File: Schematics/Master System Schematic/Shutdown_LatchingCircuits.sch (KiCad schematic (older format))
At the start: 6 parts, among them K1 3PoleSwitchingRelay, K2 3PoleSwitchingRelay, SW5 IMD_LatchReset, SW6 BMS_LatchReset

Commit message: General cleanup, and fixes
>Shutdown latch circuits updated
>Shutdown latch resets updated
>BMS cleaned up
>Some wire runs cleaned up
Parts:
- removed SW5: IMD_LatchReset, symbol Switch:SW_Push
- removed SW6: BMS_LatchReset, symbol Switch:SW_Push
- added R? (x2): 500, symbol Device:R
- D1, D2: symbol Diode:1N4001 -> LatchingFaultBoard-rescue:1N4001-Diode-Shutdown-rescue
- K1, K2: symbol NER:3PoleSwitchingRelay -> LatchingFaultBoard-rescue:3PoleSwitchingRelay-FSAE_Components-Shutdown-rescue
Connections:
- net IMDErrorIndicatorControl_OUT is gone; now on net GLV+_Fused: K1.9
- net IMD_Latch_Reset-: now reaches D1.1 (K), K1.1, K1.5
- net BMS_Latch_Reset-: now reaches D2.1 (K), K2.1, K2.5
- net BMSErrorIndicatorControl_IN: no longer names the net of K2.10
- net BMSErrorIndicatorControl_IN: now also R?.1
- net BMSErrorIndicatorControl_OUT renamed GLV+_Fused
- net BMS_Status renamed BMS_Latch_Reset+
- net IMDErrorIndicatorControl_IN: no longer names the net of K1.10
- net IMDErrorIndicatorControl_IN: now also R?.1
- net IMD_Status renamed IMD_Latch_Reset+
- net ShutdownLatch_Control_IN renamed Shutdown_OUT
- net ShutdownLatch_Control_OUT renamed Shutdown_IN
- new net BMS_Fault_Indicator: R?.2
- new net IMD_Fault_Indicator: R?.2
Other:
- note added: "Latching Fault Circuit PCB"
- note removed: "Active-High Output Relay Latch"
- moved on the sheet: D1, D2, K1, K2

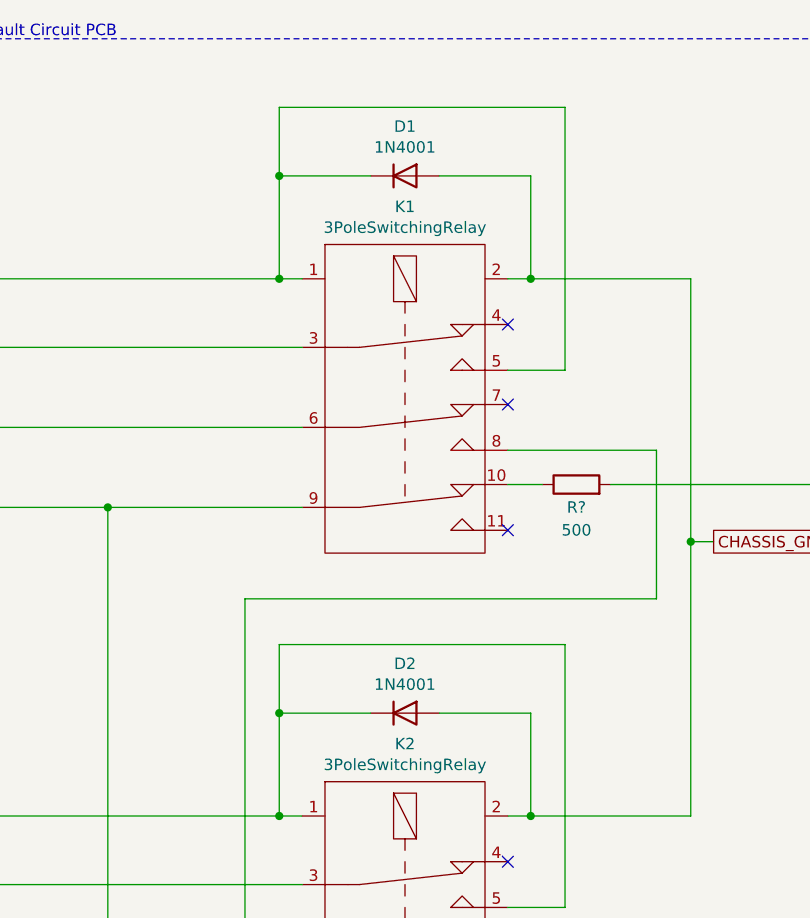
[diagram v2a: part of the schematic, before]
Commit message: Fixed symbol library issues
>Migrated 3polerelay to NER and replaced in schematic
>Used built in Diode instead of custom diode
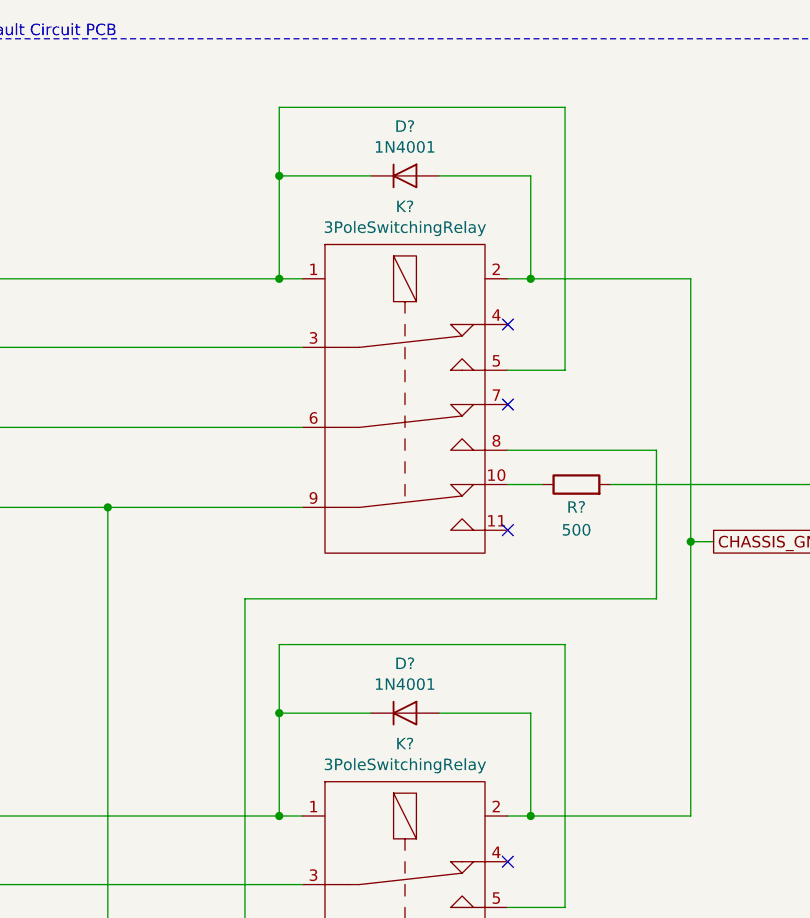
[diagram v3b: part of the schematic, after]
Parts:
- removed D1, D2: 1N4001, Diode_THT:D_DO-41_SOD81_P10.16mm_Horizontal, symbol LatchingFaultBoard-rescue:1N4001-Diode-Shutdown-rescue
- removed K1, K2: 3PoleSwitchingRelay, symbol LatchingFaultBoard-rescue:3PoleSwitchingRelay-FSAE_Components-Shutdown-rescue
- added D? (x2): 1N4001, Diode_THT:D_DO-41_SOD81_P10.16mm_Horizontal, symbol Diode:1N4001
- added K? (x2): 3PoleSwitchingRelay, symbol NER:3PoleSwitchingRelay
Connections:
- net BMS_Latch_Reset+: now also K?.3
- net BMS_Latch_Reset-: now also D?.1 (K), K?.1, K?.5
- net CHASSIS_GND: now also D?.2 (A), D?.2 (A), K?.2, K?.2
- net GLV+_Fused: now also K?.9, K?.9
- net IMD_Latch_Reset+: now also K?.3
- net IMD_Latch_Reset-: now also D?.1 (K), K?.1, K?.5
- net Shutdown_IN: now also K?.6
- net Shutdown_OUT: now also K?.8
- net at R?.1: now also K?.10 (x2)
- new net: K?.6, K?.8
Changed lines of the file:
@@
 Wire Wire Line
 	4800 2850 5050 2850
-$Comp
-L LatchingFaultBoard-rescue:1N4001-Diode-Shutdown-rescue D1
-U 1 1 5DDE3BD5
-P 4350 2000
-F 0 "D1" H 4350 2216 50  0000 C CNN
-F 1 "1N4001" H 4350 2125 50  0000 C CNN
-F 2 "Diode_THT:D_DO-41_SOD81_P10.16mm_Horizontal" H 4350 1825 50  0001 C CNN
-F 3 "http://www.vishay.com/docs/88503/1n4001.pdf" H 4350 2000 50  0001 C CNN
-	1    4350 2000
-	1    0    0    -1
-$EndComp
 Wire Wire Line
 	3800 2000 4200 2000
@@
 Wire Wire Line
 	3800 1700 5050 1700
-$Comp
-L LatchingFaultBoard-rescue:3PoleSwitchingRelay-FSAE_Components-Shutdown-rescue K2
-U 1 1 5DE0D324
-P 4350 4600
-F 0 "K2" H 4350 4715 50  0000 C CNN
-F 1 "3PoleSwitchingRelay" H 4350 4624 50  0000 C CNN
-F 2 "" H 4350 4600 50  0001 C CNN
-F 3 "" H 4350 4600 50  0001 C CNN
-	1    4350 4600
-	1    0    0    -1
-$EndComp
 Wire Wire Line
 	4800 5200 5050 5200
-$Comp
-L LatchingFaultBoard-rescue:1N4001-Diode-Shutdown-rescue D2
-U 1 1 5DE0D338
-P 4350 4350
-F 0 "D2" H 4350 4566 50  0000 C CNN
-F 1 "1N4001" H 4350 4475 50  0000 C CNN
-F 2 "Diode_THT:D_DO-41_SOD81_P10.16mm_Horizontal" H 4350 4175 50  0001 C CNN
-F 3 "http://www.vishay.com/docs/88503/1n4001.pdf" H 4350 4350 50  0001 C CNN
-	1    4350 4350
-	1    0    0    -1
-$EndComp
 Wire Wire Line
 	3800 4050 3800 4350
@@
 Wire Wire Line
 	3800 4050 5050 4050
-$Comp
-L LatchingFaultBoard-rescue:3PoleSwitchingRelay-FSAE_Components-Shutdown-rescue K1
-U 1 1 5DDDA065
-P 4350 2250
-F 0 "K1" H 4350 2365 50  0000 C CNN
-F 1 "3PoleSwitchingRelay" H 4350 2274 50  0000 C CNN
-F 2 "" H 4350 2250 50  0001 C CNN
-F 3 "" H 4350 2250 50  0001 C CNN
-	1    4350 2250
-	1    0    0    -1
-$EndComp
 $Comp
 L Device:R R?
@@
 Wire Wire Line
 	5600 3600 5600 4800
+$Comp
+L Diode:1N4001 D?
+U 1 1 5F682B6B
+P 4350 2000
+F 0 "D?" H 4350 2216 50  0000 C CNN
+F 1 "1N4001" H 4350 2125 50  0000 C CNN
+F 2 "Diode_THT:D_DO-41_SOD81_P10.16mm_Horizontal" H 4350 1825 50  0001 C CNN
+F 3 "http://www.vishay.com/docs/88503/1n4001.pdf" H 4350 2000 50  0001 C CNN
+	1    4350 2000
+	1    0    0    -1
+$EndComp
+$Comp
+L Diode:1N4001 D?
+U 1 1 5F684662
+P 4350 4350
+F 0 "D?" H 4350 4566 50  0000 C CNN
+F 1 "1N4001" H 4350 4475 50  0000 C CNN
+F 2 "Diode_THT:D_DO-41_SOD81_P10.16mm_Horizontal" H 4350 4175 50  0001 C CNN
+F 3 "http://www.vishay.com/docs/88503/1n4001.pdf" H 4350 4350 50  0001 C CNN
+	1    4350 4350
+	1    0    0    -1
+$EndComp
+$Comp
+L NER:3PoleSwitchingRelay K?
+U 1 1 5F6868C5
+P 4350 2250
+F 0 "K?" H 4350 2365 50  0000 C CNN
+F 1 "3PoleSwitchingRelay" H 4350 2274 50  0000 C CNN
+F 2 "" H 4350 2250 50  0001 C CNN
+F 3 "" H 4350 2250 50  0001 C CNN
+	1    4350 2250
+	1    0    0    -1
+$EndComp
+$Comp
+L NER:3PoleSwitchingRelay K?
+U 1 1 5F68C6F6
+P 4350 4600
+F 0 "K?" H 4350 4715 50  0000 C CNN
+F 1 "3PoleSwitchingRelay" H 4350 4624 50  0000 C CNN
+F 2 "" H 4350 4600 50  0001 C CNN
+F 3 "" H 4350 4600 50  0001 C CNN
+	1    4350 4600
+	1    0    0    -1
+$EndComp
 $EndSCHEMATC

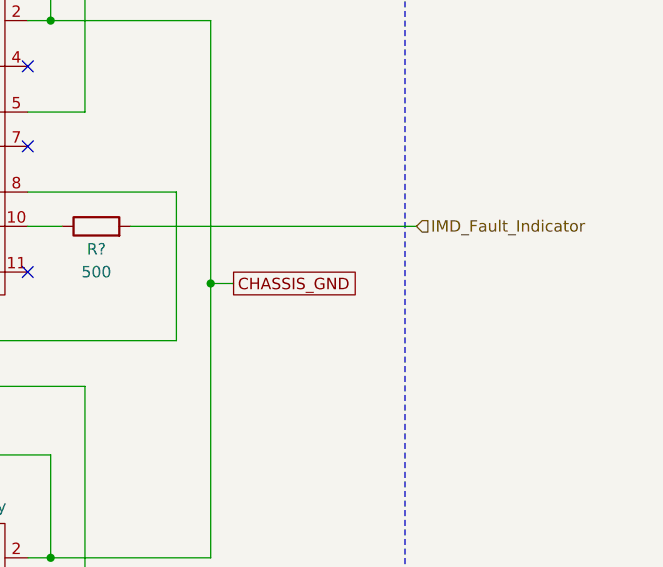
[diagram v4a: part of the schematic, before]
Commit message: More cleanup and detangling
>Detangled wires
>Improved spacing
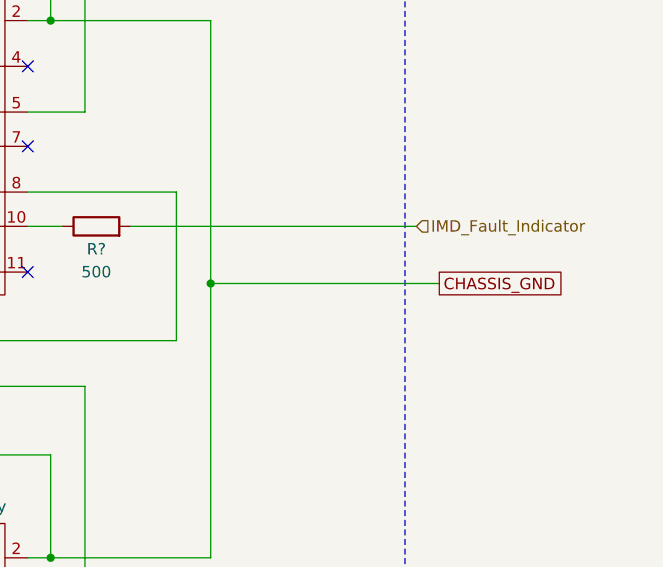
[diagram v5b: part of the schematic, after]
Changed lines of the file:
@@
 Text HLabel 6500 5550 2    50   Input ~ 0
 Shutdown_OUT
-Text GLabel 5700 3600 2    50   UnSpc ~ 0
+Text GLabel 6600 3600 2    50   UnSpc ~ 0
 CHASSIS_GND
 Text HLabel 6500 3350 2    50   Input ~ 0
@@
 Wire Wire Line
 	5600 2450 5600 3600
-Wire Wire Line
-	5700 3600 5600 3600
 Connection ~ 5600 3600
 Wire Wire Line
@@
 	1    0    0    -1
 $EndComp
+Wire Wire Line
+	5600 3600 6600 3600
 $EndSCHEMATC
